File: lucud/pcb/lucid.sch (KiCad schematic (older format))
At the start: 1 part, among them J2 Conn_02x30_Odd_Even

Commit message: Worked on the PCB
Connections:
- net I.1: now reaches J2.10 (Pin_10)
- net O.2: now reaches J2.11 (Pin_11)
- net I.2: now reaches J2.12 (Pin_12)
- net O.3: now reaches J2.13 (Pin_13)
- net I.3: now reaches J2.14 (Pin_14)
- net O.4: now reaches J2.15 (Pin_15)
- net I.4: now reaches J2.16 (Pin_16)
- net O.5: now reaches J2.17 (Pin_17)
- net I.5: now reaches J2.18 (Pin_18)
- net O.6: now reaches J2.19 (Pin_19)
- net I.6: now reaches J2.20 (Pin_20)
- net O.7: now reaches J2.21 (Pin_21)
- net I.7: now reaches J2.22 (Pin_22)
- net O.8: now reaches J2.23 (Pin_23)
- net I.8: now reaches J2.24 (Pin_24)
- net 0.9: now reaches J2.25 (Pin_25)
- net I.9: now reaches J2.26 (Pin_26)
- net O.10: now reaches J2.27 (Pin_27)
- net I.10: now reaches J2.28 (Pin_28)
- net O.11: now reaches J2.29 (Pin_29)
- net I.11: now reaches J2.30 (Pin_30)
- net O.12: now reaches J2.31 (Pin_31)
- net I.12: now reaches J2.32 (Pin_32)
- net O.13: now reaches J2.33 (Pin_33)
- net I.13: now reaches J2.34 (Pin_34)
- net O.14: now reaches J2.35 (Pin_35)
- net I.14: now reaches J2.36 (Pin_36)
- net O.15: now reaches J2.37 (Pin_37)
- net I.15: now reaches J2.38 (Pin_38)
- net D0: now reaches J2.39 (Pin_39)
- net B0: now reaches J2.40 (Pin_40)
- net D1: now reaches J2.41 (Pin_41)
- net B1: now reaches J2.42 (Pin_42)
- net D2: now reaches J2.43 (Pin_43)
- net B2: now reaches J2.44 (Pin_44)
- net D3: now reaches J2.45 (Pin_45)
- net B3: now reaches J2.46 (Pin_46)
- net D4: now reaches J2.47 (Pin_47)
- net D5: now reaches J2.49 (Pin_49)
- net BOOT_PB: now reaches J2.50 (Pin_50)
- net D6: now reaches J2.51 (Pin_51)
- net USB_D-: now reaches J2.52 (Pin_52)
- net D7: now reaches J2.53 (Pin_53)
- net USB_D+: now reaches J2.54 (Pin_54)
- net SWD_DAT: now reaches J2.56 (Pin_56)
- net SWD_CLK: now reaches J2.58 (Pin_58)
- net nRST: now reaches J2.60 (Pin_60)
- net O.0: now reaches J2.7 (Pin_7)
- net O.1: now reaches J2.9 (Pin_9)
- net Buffer/DI.0 renamed I.0
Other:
- note added: "Need another 4x analog inputs."
- moved on the sheet: J2

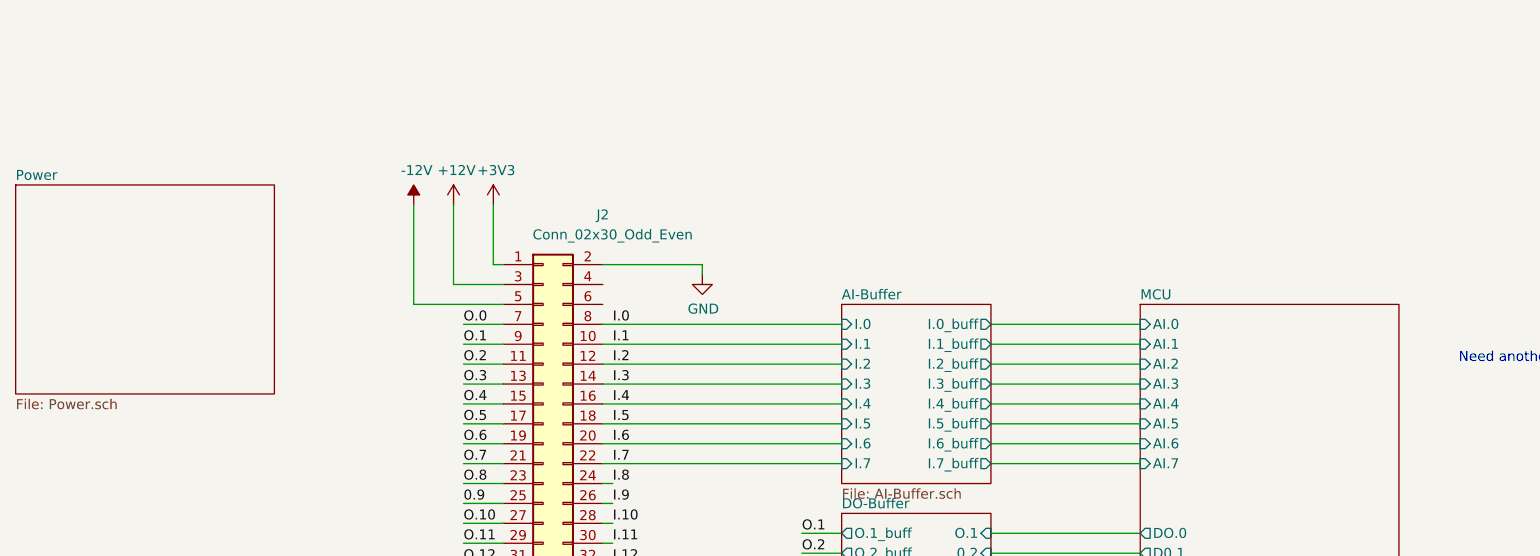
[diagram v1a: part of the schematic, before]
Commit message: Added buffer parts
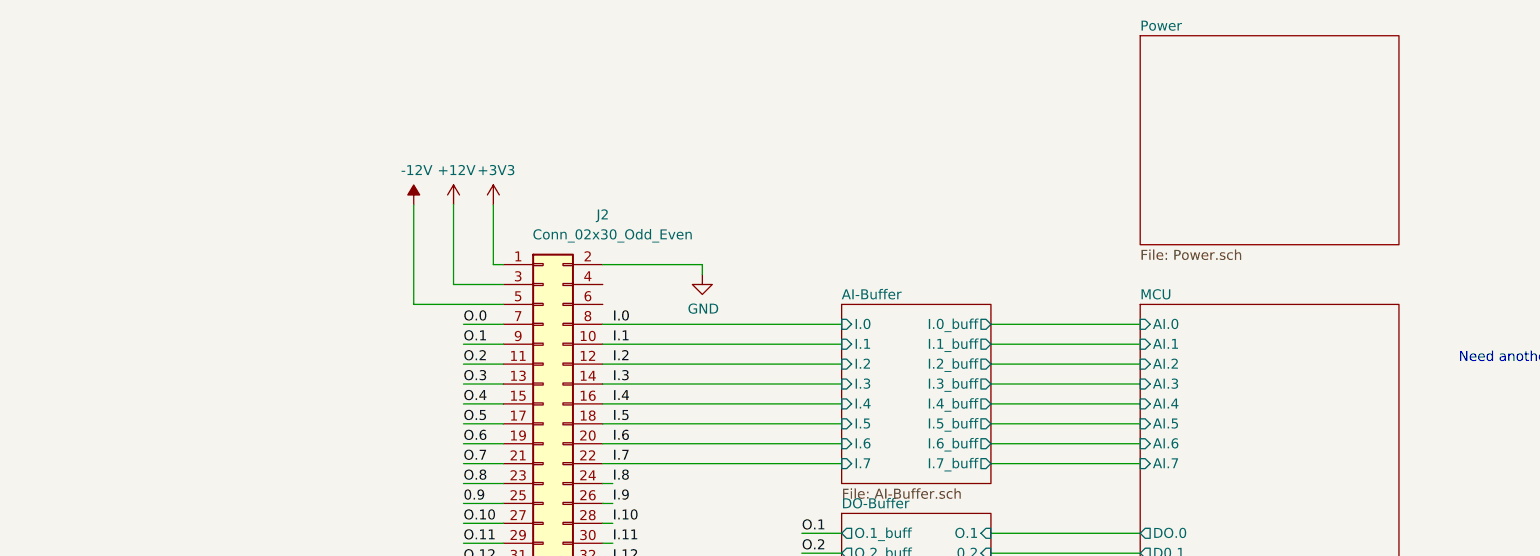
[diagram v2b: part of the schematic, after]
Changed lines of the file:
@@
 $EndSheet
 $Sheet
-S 1850 1500 1300 1050
+S 7500 750  1300 1050
 U 5C243B4D
 F0 "Power" 50

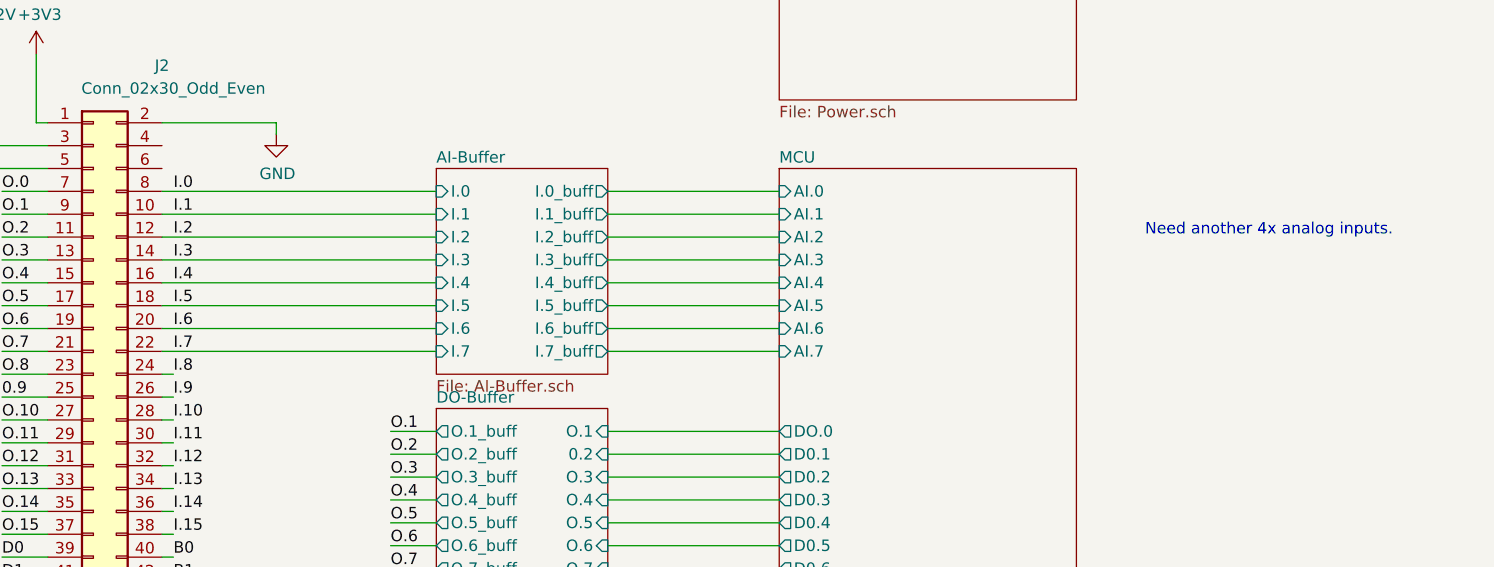
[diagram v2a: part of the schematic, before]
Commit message: Finished the first crack at the drum module
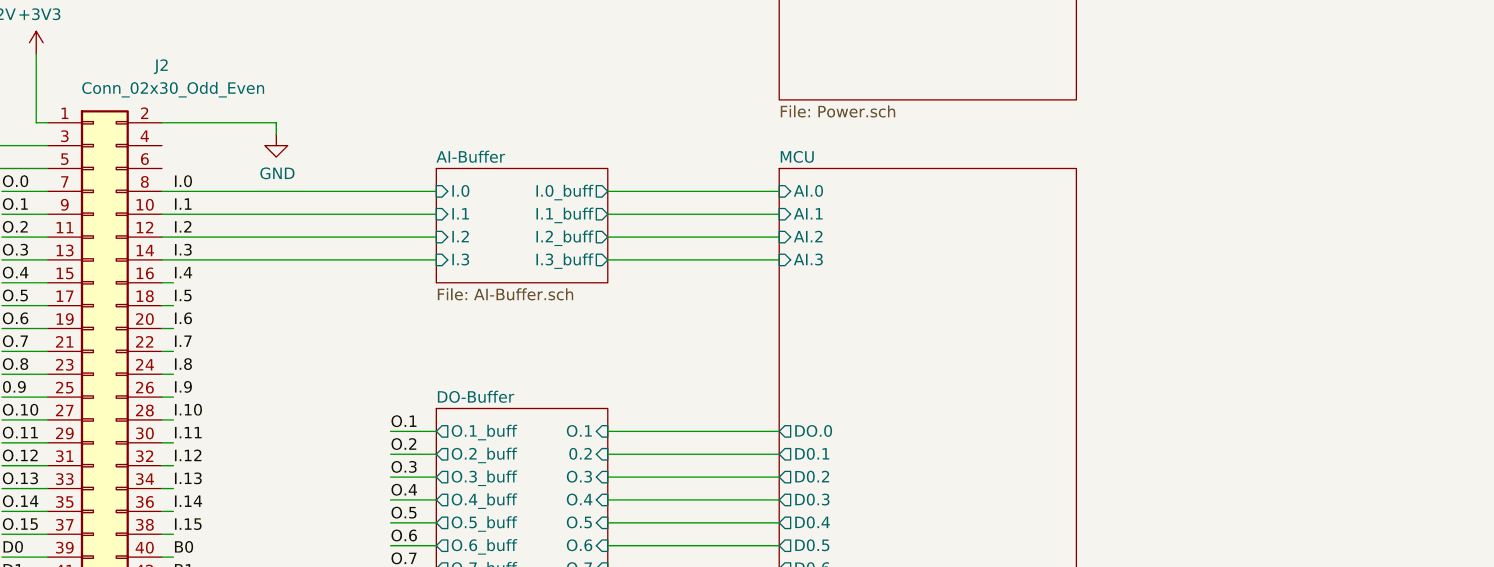
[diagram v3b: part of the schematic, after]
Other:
- note removed: "Need another 4x analog inputs."
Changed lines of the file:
@@
 F4 "AI.2" I L 7500 2400 50
 F5 "AI.3" I L 7500 2500 50
-F6 "AI.4" I L 7500 2600 50
-F7 "AI.5" I L 7500 2700 50
-F8 "AI.6" I L 7500 2800 50
-F9 "AI.7" I L 7500 2900 50
-F10 "DO.0" O L 7500 3250 50
-F11 "D0.1" O L 7500 3350 50
-F12 "D0.2" O L 7500 3450 50
-F13 "D0.3" O L 7500 3550 50
-F14 "D0.4" O L 7500 3650 50
-F15 "D0.5" O L 7500 3750 50
-F16 "D0.6" O L 7500 3850 50
-F17 "D0.7" O L 7500 3950 50
-F18 "BOOT_PB" I L 7500 4300 50
-F19 "USB_D-" I L 7500 4400 50
-F20 "USB_D+" I L 7500 4500 50
-F21 "SWD_CLK" I L 7500 4600 50
-F22 "SWD_DAT" I L 7500 4700 50
-F23 "nRST" I L 7500 4800 50
+F6 "DO.0" O L 7500 3250 50
+F7 "D0.1" O L 7500 3350 50
+F8 "D0.2" O L 7500 3450 50
+F9 "D0.3" O L 7500 3550 50
+F10 "D0.4" O L 7500 3650 50
+F11 "D0.5" O L 7500 3750 50
+F12 "D0.6" O L 7500 3850 50
+F13 "D0.7" O L 7500 3950 50
+F14 "BOOT_PB" I L 7500 4300 50
+F15 "USB_D-" I L 7500 4400 50
+F16 "USB_D+" I L 7500 4500 50
+F17 "SWD_CLK" I L 7500 4600 50
+F18 "SWD_DAT" I L 7500 4700 50
+F19 "nRST" I L 7500 4800 50
 $EndSheet
 $Sheet
@@
 $EndComp
 $Sheet
-S 6000 2100 750  900
+S 6000 2100 750  500
 U 5C2657C1
 F0 "AI-Buffer" 50
@@
 F4 "I.2" I L 6000 2400 50
 F5 "I.3" I L 6000 2500 50
-F6 "I.4" I L 6000 2600 50
-F7 "I.5" I L 6000 2700 50
-F8 "I.6" I L 6000 2800 50
-F9 "I.7" I L 6000 2900 50
-F10 "I.0_buff" O R 6750 2200 50
-F11 "I.1_buff" O R 6750 2300 50
-F12 "I.3_buff" O R 6750 2500 50
-F13 "I.4_buff" O R 6750 2600 50
-F14 "I.2_buff" O R 6750 2400 50
-F15 "I.5_buff" O R 6750 2700 50
-F16 "I.6_buff" O R 6750 2800 50
-F17 "I.7_buff" O R 6750 2900 50
+F6 "I.0_buff" O R 6750 2200 50
+F7 "I.1_buff" O R 6750 2300 50
+F8 "I.3_buff" O R 6750 2500 50
+F9 "I.2_buff" O R 6750 2400 50
 $EndSheet
 Wire Wire Line
@@
 	6000 2500 4800 2500
 Wire Wire Line
-	4800 2600 6000 2600
-Wire Wire Line
-	6000 2700 4800 2700
-Wire Wire Line
-	4800 2800 6000 2800
-Wire Wire Line
-	6000 2900 4800 2900
-Wire Wire Line
 	4800 2300 6000 2300
 Wire Wire Line
@@
 Wire Wire Line
 	6750 2500 7500 2500
-Wire Wire Line
-	6750 2600 7500 2600
-Wire Wire Line
-	6750 2700 7500 2700
-Wire Wire Line
-	6750 2800 7500 2800
-Wire Wire Line
-	6750 2900 7500 2900
 $Sheet
 S 6000 3150 750  900
@@
 Wire Wire Line
 	4800 4800 7500 4800
-Text Notes 9100 2400 0    50   ~ 0
-Need another 4x analog inputs.
+Wire Wire Line
+	4850 2600 4800 2600
+Wire Wire Line
+	4800 2700 4850 2700
+Wire Wire Line
+	4850 2800 4800 2800
+Wire Wire Line
+	4800 2900 4850 2900
 $EndSCHEMATC
